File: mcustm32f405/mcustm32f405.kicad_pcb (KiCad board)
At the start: 2 copper layers, 76.2 x 50.8 mm, 36 parts, among them J2 STM32WORLD_BASE, SW1 TS-1088R-02526, SW2 TS-1088R-02526, U1 AMS1117-3.3, U2 SRV05-4, U3 STM32F405RGTx, Y1 X_16MHZ

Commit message: Hmmm
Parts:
- removed the R3 at (174.6, 102.9)
- removed the R4 at (174.6, 101.0)
- moved R2 3.86 mm to (178.4, 98.4)
- moved R1 3.81 mm to (178.4, 104.8)
- renumbered R5 to R3, R6 to R4, R7 to R5, R8 to R6
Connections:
- J1 pad A6: Net-(J1-PadA6) -> PA12
- J1 pad A7: Net-(J1-PadA7) -> PA11
- J1 pad B6: Net-(J1-PadA6) -> PA12
- J1 pad B7: Net-(J1-PadA7) -> PA11
- R1 pad 1: PC14 -> GND
- R2 pad 1: PC14 -> GND
- U2 pad 1: Net-(J1-PadA6) -> PA12
- U2 pad 3: Net-(J1-PadA7) -> PA11
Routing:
- net PC14: track 61.8 -> 24.7 mm, vias 2 -> 0
- net PA12: track 36.0 -> 47.9 mm
- net PA11: track 34.3 -> 45.9 mm
- net Net-(J1-PadA7): track 10.8 -> 0.00 mm
- net Net-(J1-PadA6): track 10.8 -> 0.00 mm
- net Net-(J1-PadB5): track 7.52 -> 3.98 mm
- net Net-(J1-PadA5): track 7.99 -> 4.52 mm
- net PA8: track 29.4 -> 30.9 mm
- net PA9: track 24.9 -> 26.0 mm
- net PA10: track 26.5 -> 27.2 mm
- net GND: vias 16 -> 18

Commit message: Hmmmm
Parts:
- turned JP1 to 0 degrees
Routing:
- net PC13: track 37.6 -> 51.5 mm, vias 1 -> 0
- net VBAT: track 37.9 -> 42.1 mm, vias 2 -> 1
- net +3V3: track 206.1 -> 202.5 mm
- net BO0: track 58.3 -> 60.0 mm
- net Net-(C14-Pad1): track 2.46 -> 3.54 mm
- net GND: vias 18 -> 21
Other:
- board text added: "VBAT"
- board text added: "VDDA"

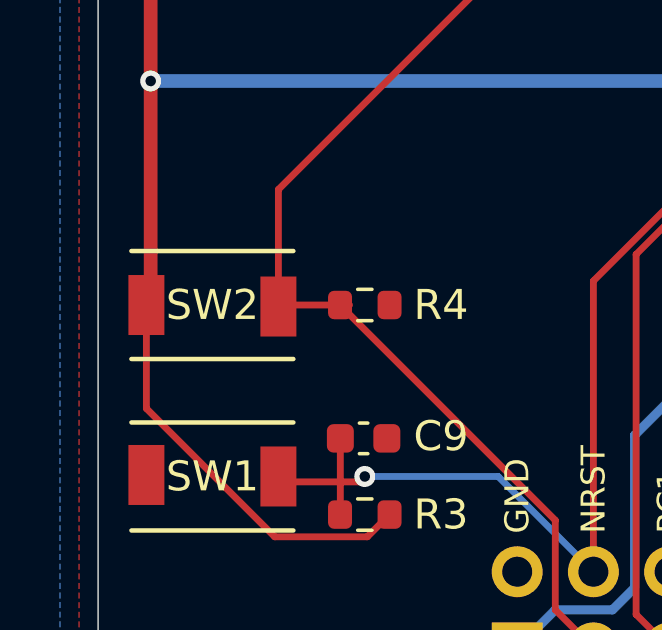
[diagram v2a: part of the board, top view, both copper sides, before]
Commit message: Changing connector symbol and footprints
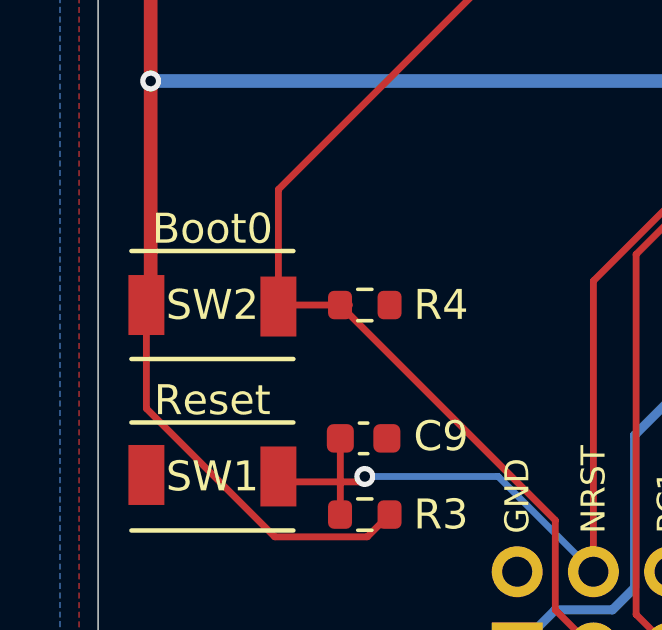
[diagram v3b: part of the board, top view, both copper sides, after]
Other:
- board text added: "Boot0"
- board text added: "Reset"
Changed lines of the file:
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@@
     (effects (font (size 1 1) (thickness 0.15)) (justify mirror))
+  )
+  (gr_text "Reset" (at 118.11 113.665) (layer "F.SilkS")
+    (effects (font (size 1 1) (thickness 0.15)))
+  )
+  (gr_text "Boot0" (at 118.11 107.95) (layer "F.SilkS")
+    (effects (font (size 1 1) (thickness 0.15)))
   )
   (dimension (type aligned) (layer "Dwgs.User")

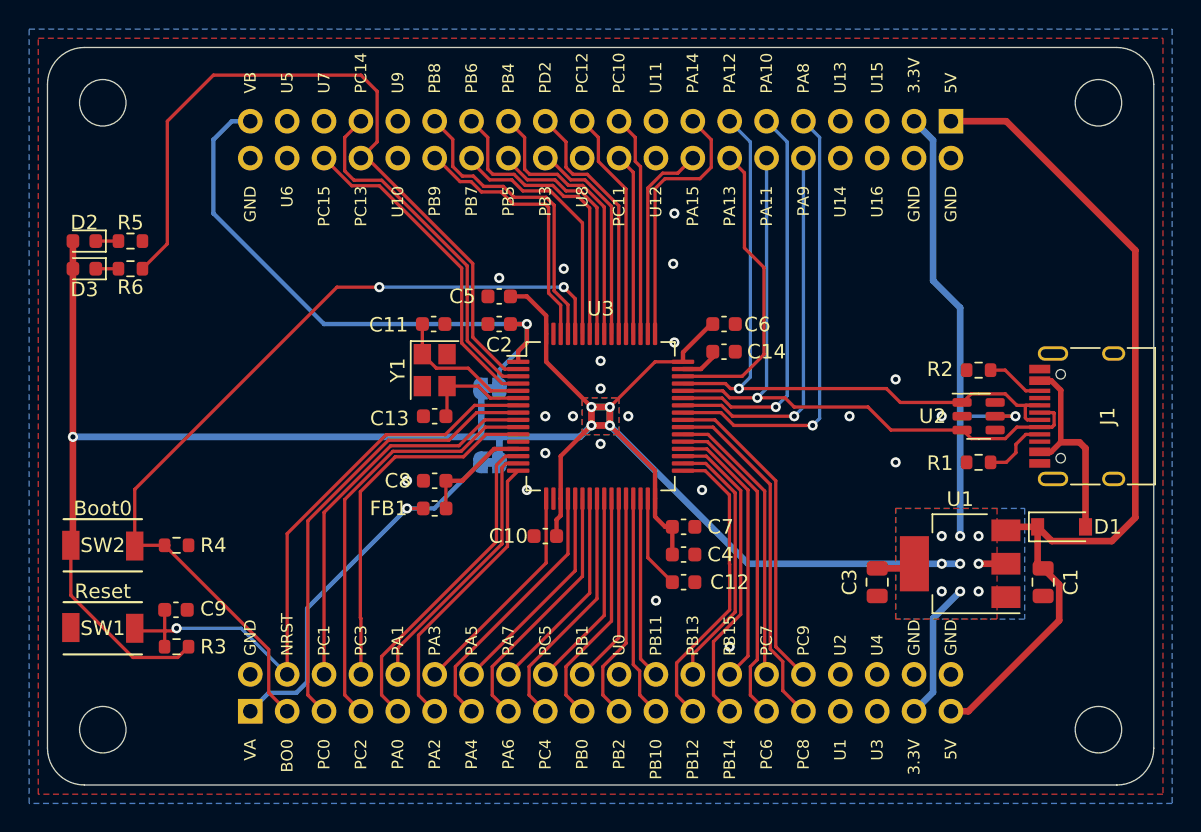
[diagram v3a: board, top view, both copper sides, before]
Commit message: MCUSTM32F405 should be ready for order
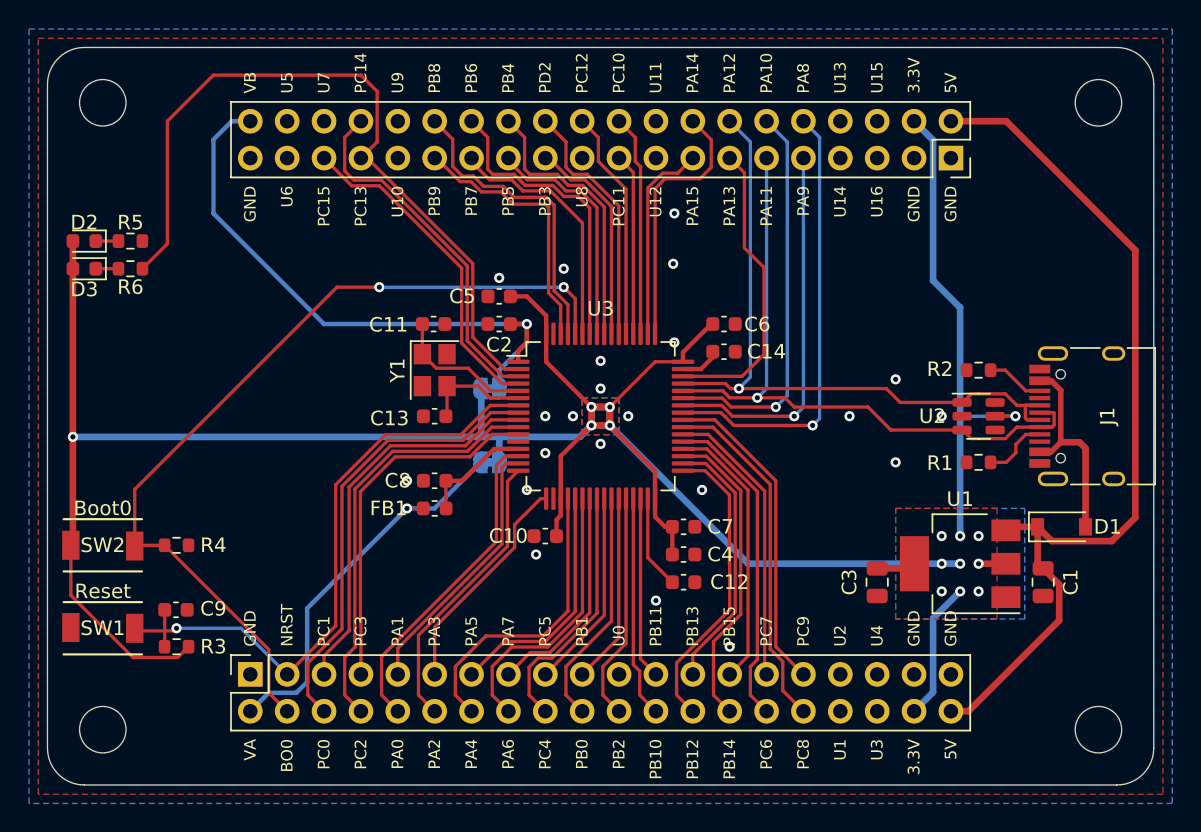
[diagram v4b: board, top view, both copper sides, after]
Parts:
- added J3: STM32WORLD_CONNECTOR_2, stm32world:PinSocket_2x20_P2.54mm_Vertical_Stackable, F.Cu at (176.5, 83.8)
- added J4: STM32WORLD_BOARD, stm32world:STM32WORLD_BOARD, F.Cu at (152.4, 101.6)
- J2: value STM32WORLD_BASE -> STM32WORLD_CONNECTOR_1; footprint stm32world:STM32WORLD_BASE -> stm32world:PinSocket_2x20_P2.54mm_Vertical_Stackable
- moved J2 30.0 mm to (128.3, 119.4), turned to 90 degrees
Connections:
- J2 pad 1: VDDA -> GND
- J2 pad 10: PA1 -> PA0
- J2 pad 11: PA2 -> PA3
- J2 pad 12: PA3 -> PA2
- J2 pad 13: PA4 -> PA5
- J2 pad 14: PA5 -> PA4
- J2 pad 15: PA6 -> PA7
- J2 pad 16: PA7 -> PA6
- J2 pad 17: PC4 -> PC5
- J2 pad 18: PC5 -> PC4
- J2 pad 19: PB0 -> PB1
- J2 pad 2: GND -> VDDA
- J2 pad 20: PB1 -> PB0
- J2 pad 21: PB2 -> unconnected-(J2-Pad21)
- J2 pad 22: unconnected-(J2-Pad22) -> PB2
- J2 pad 23: PB10 -> PB11
- J2 pad 24: PB11 -> PB10
- J2 pad 25: PB12 -> PB13
- J2 pad 26: PB13 -> PB12
- J2 pad 27: PB14 -> PB15
- J2 pad 28: PB15 -> PB14
- J2 pad 29: PC6 -> PC7
- J2 pad 3: BO0 -> NRST
- J2 pad 30: PC7 -> PC6
- J2 pad 31: PC8 -> PC9
- J2 pad 32: PC9 -> PC8
- J2 pad 37: +3V3 -> GND
- J2 pad 38: GND -> +3V3
- J2 pad 39: +5V -> GND
- J2 pad 4: NRST -> BO0
- J2 pad 40: GND -> +5V
- J2 pad 5: PC0 -> PC1
- J2 pad 6: PC1 -> PC0
- J2 pad 7: PC2 -> PC3
- J2 pad 8: PC3 -> PC2
- J2 pad 9: PA0 -> PA1
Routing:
- net PA4: track 18.3 -> 20.6 mm
- net PA5: track 15.1 -> 16.7 mm
- net PA6: track 17.7 -> 19.1 mm
- net PA7: track 14.4 -> 15.2 mm
- net Net-(C14-Pad1): track 3.54 -> 2.77 mm
- net PC4: track 17.0 -> 17.6 mm
- net GND: vias 21 -> 22

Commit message: Hmmmm
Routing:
- net PB4: track 19.1 -> 18.1 mm
- net PB5: track 16.1 -> 15.5 mm
- net PB6: track 20.6 -> 19.9 mm
- net PD2: track 17.3 -> 16.7 mm
- net PB3: track 14.5 -> 13.9 mm
- net GND: vias 22 -> 23

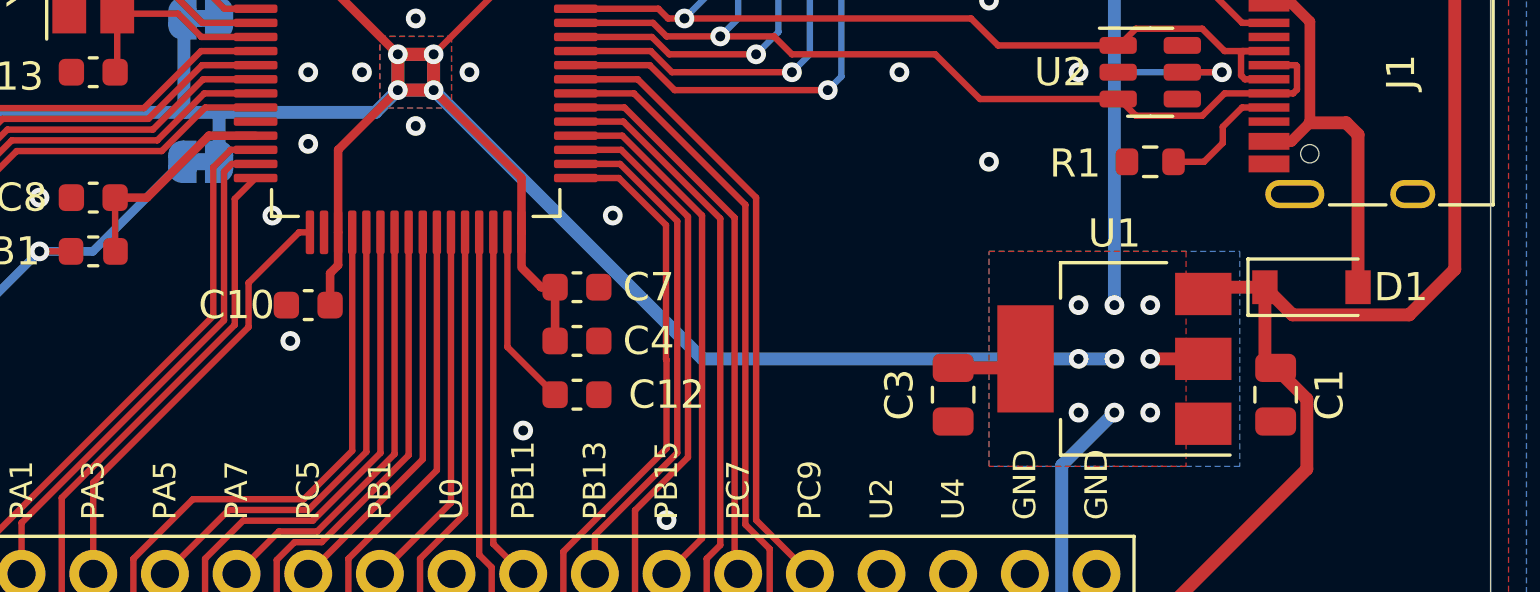
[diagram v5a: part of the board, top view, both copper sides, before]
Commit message: Ready to order mcustm32f405
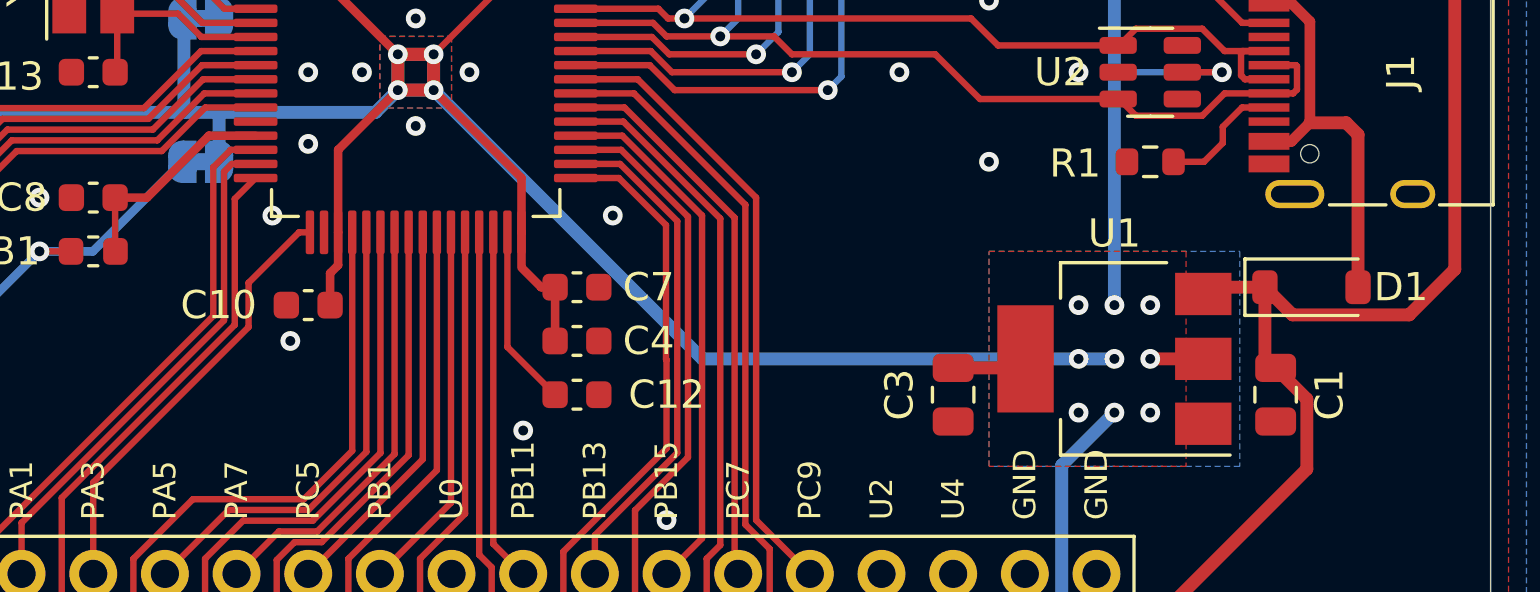
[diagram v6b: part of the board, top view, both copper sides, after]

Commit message: Hmmm
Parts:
- removed U2: SRV05-4, Package_TO_SOT_SMD:SOT-23-6
- added D4: PSM712, Package_TO_SOT_SMD:SOT-23, F.Cu at (178.7, 101.6)
- added JP3: SolderJumper_2_Bridged, Jumper:SolderJumper-2_P1.3mm_Bridged_RoundedPad1.0x1.5mm, F.Cu at (124.5, 121.3)
- added JP4: SolderJumper_2_Bridged, Jumper:SolderJumper-2_P1.3mm_Bridged_RoundedPad1.0x1.5mm, F.Cu at (124.5, 123.8)
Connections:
- J2 pad 3: NRST -> HNRST
- J2 pad 4: BO0 -> HBO0
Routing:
- net HBO0: track 0.00 -> 6.49 mm
- net HNRST: track 0.00 -> 6.49 mm
- net +3V3: track 202.3 -> 197.5 mm, vias 15 -> 14
- net NRST: track 43.5 -> 42.0 mm
- net BO0: track 60.0 -> 60.1 mm, vias 2 -> 4

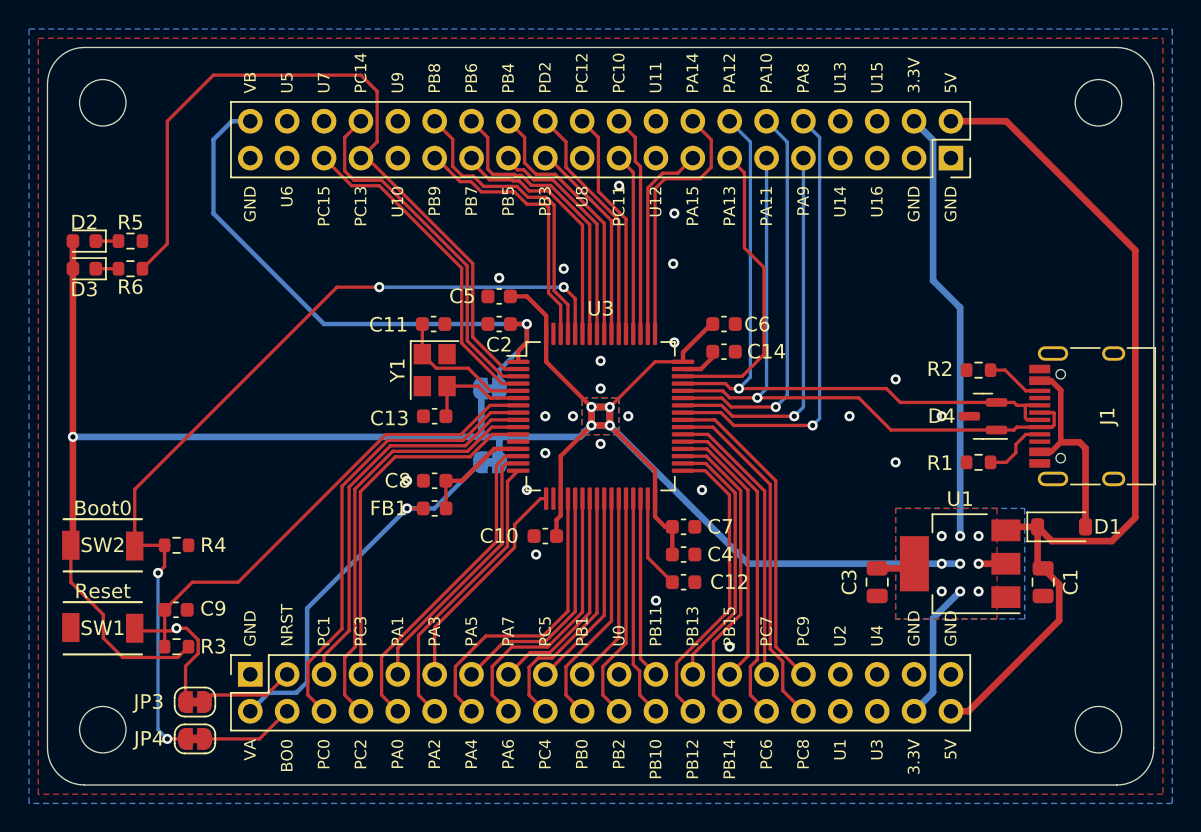
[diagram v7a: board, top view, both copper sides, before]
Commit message: Jumpers for nrst and b0 on header.
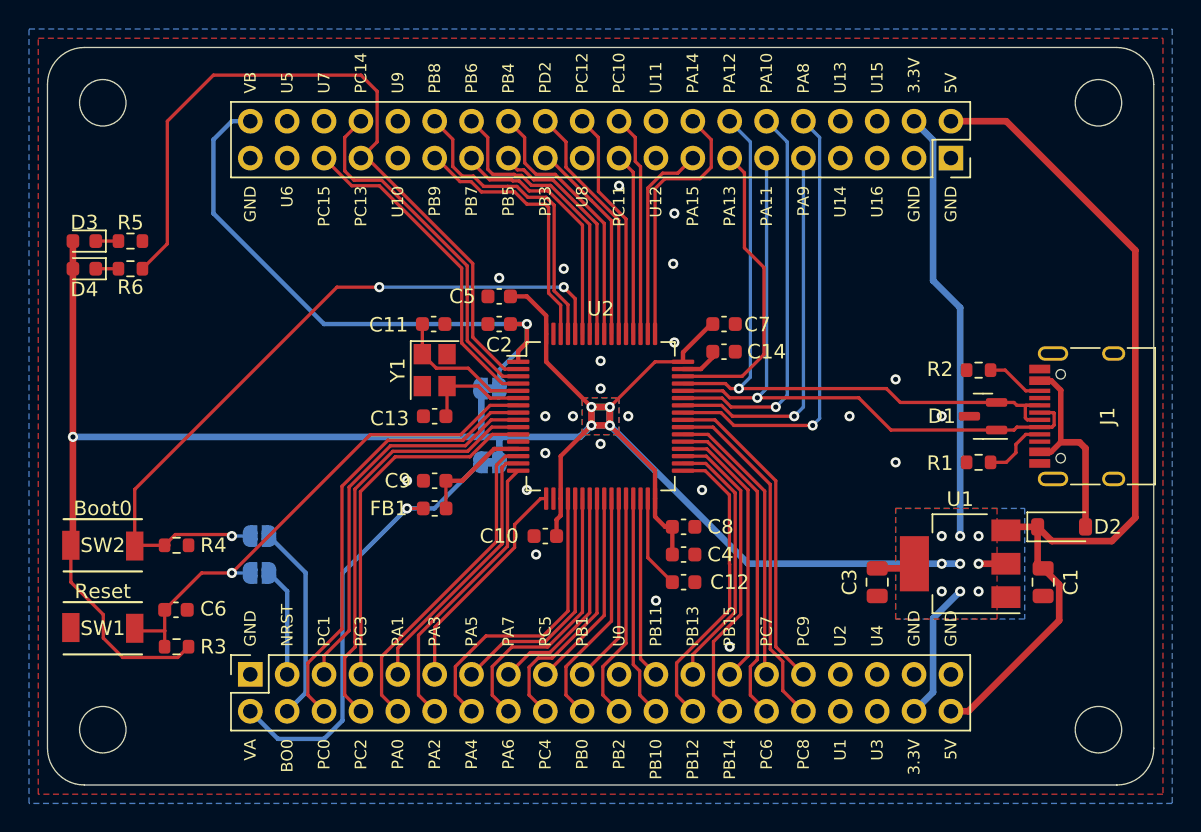
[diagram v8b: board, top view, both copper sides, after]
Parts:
- JP3, JP4: value SolderJumper_2_Bridged -> ~; footprint Jumper:SolderJumper-2_P1.3mm_Bridged_RoundedPad1.0x1.5mm -> Jumper:SolderJumper-2_P1.3mm_Open_RoundedPad1.0x1.5mm; moved to B.Cu
- moved JP4 14.7 mm to (128.9, 109.9)
- moved JP3 9.94 mm to (128.9, 112.4)
- renumbered C9 to C6, C6 to C7, C7 to C8, C8 to C9, D4 to D1, D1 to D2, D2 to D3, D3 to D4, U3 to U2
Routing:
- net BO0: track 60.1 -> 51.3 mm, vias 4 -> 3
- net HBO0: track 6.49 -> 13.6 mm
- net NRST: track 42.0 -> 35.9 mm
- net VDDA: track 27.1 -> 31.6 mm
- net HNRST: track 6.49 -> 7.50 mm
